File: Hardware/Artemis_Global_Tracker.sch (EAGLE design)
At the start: 137 parts, among them J1 IRIDIUM_9603N, J2 USB-C, J6 U.FL, J7 ANTENNA-GROUNDEDEDGE_SMA, Q1 DMG3414U-7, Q2 DMG3415U-7, Q3 DMG3415U-7, Q4 600mA/40V, U1 CH340E_MSOP10, U10 3.3V, U2 LTC3225EDDB#TRMPBF, U3 ADM4210-1, U4 UBLOX_ZOE_M8-0-10, U5 AS179-92LF, U6 MS8607-02BA01, U7 ARTEMIS_MODULESMD, U8 V_SUPERVISORBD48K24G-TL, U9 MCP73831, X1 32.768kHz, X2 32.768kHz

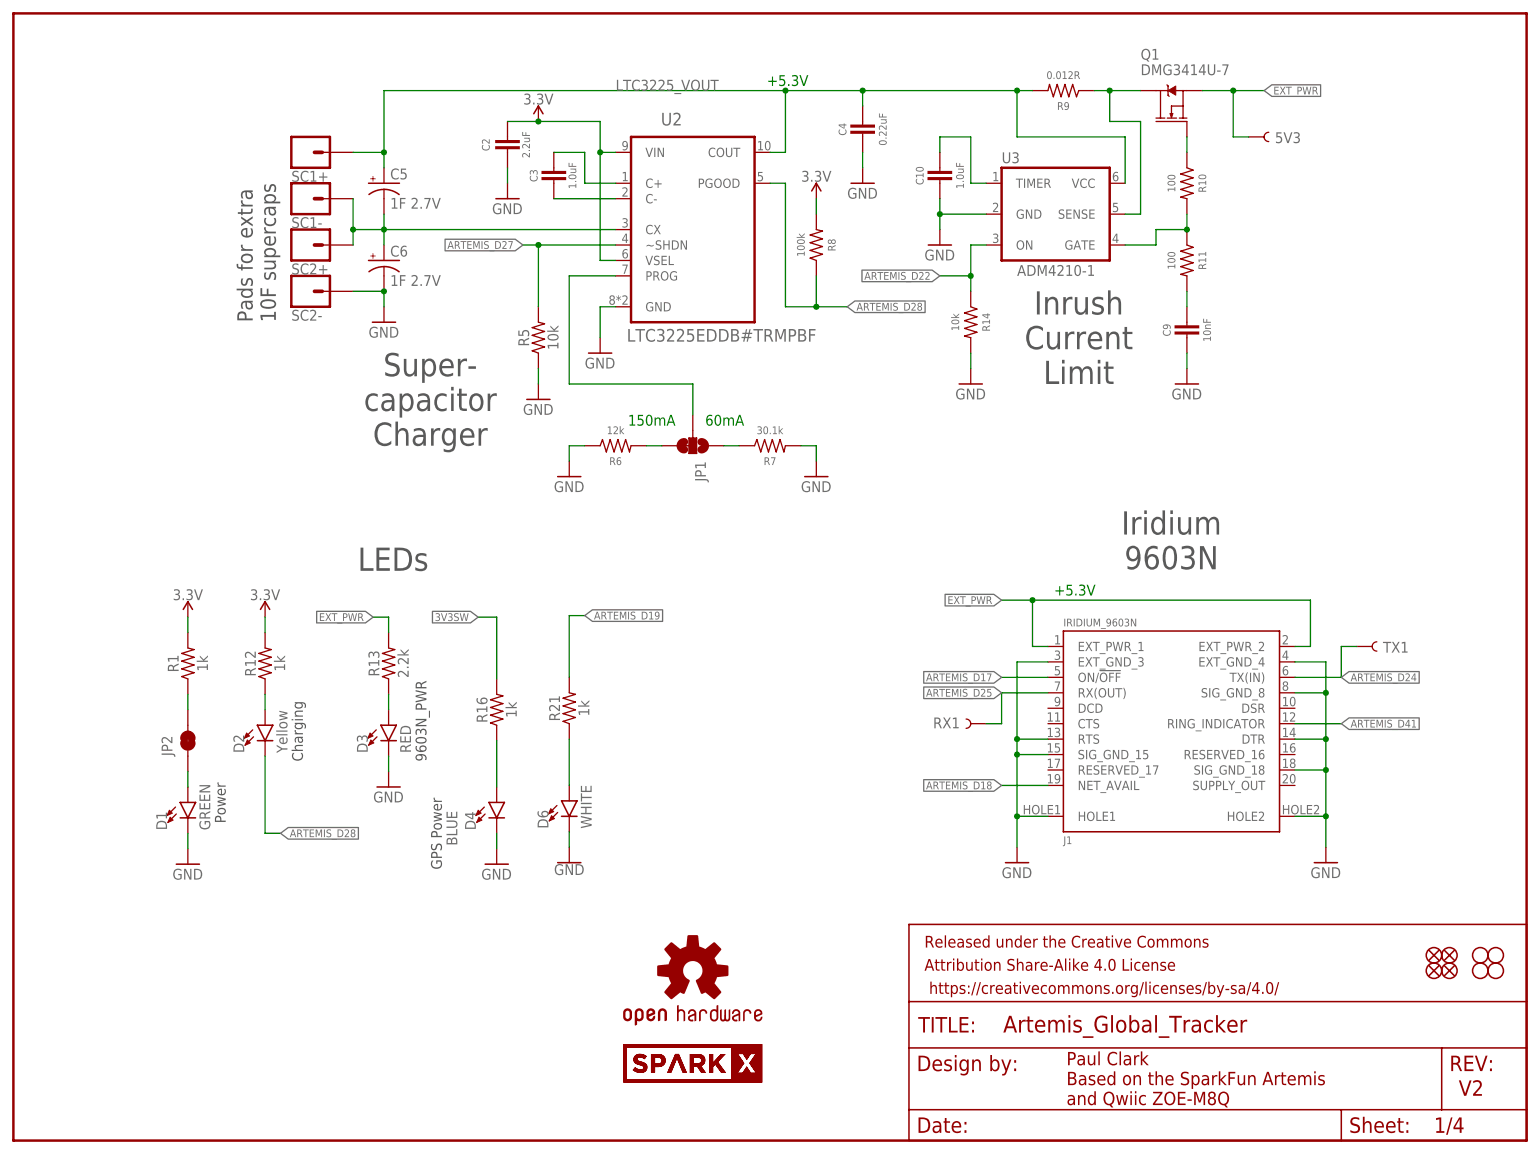
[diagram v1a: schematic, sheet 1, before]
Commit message: PROD_ID updates
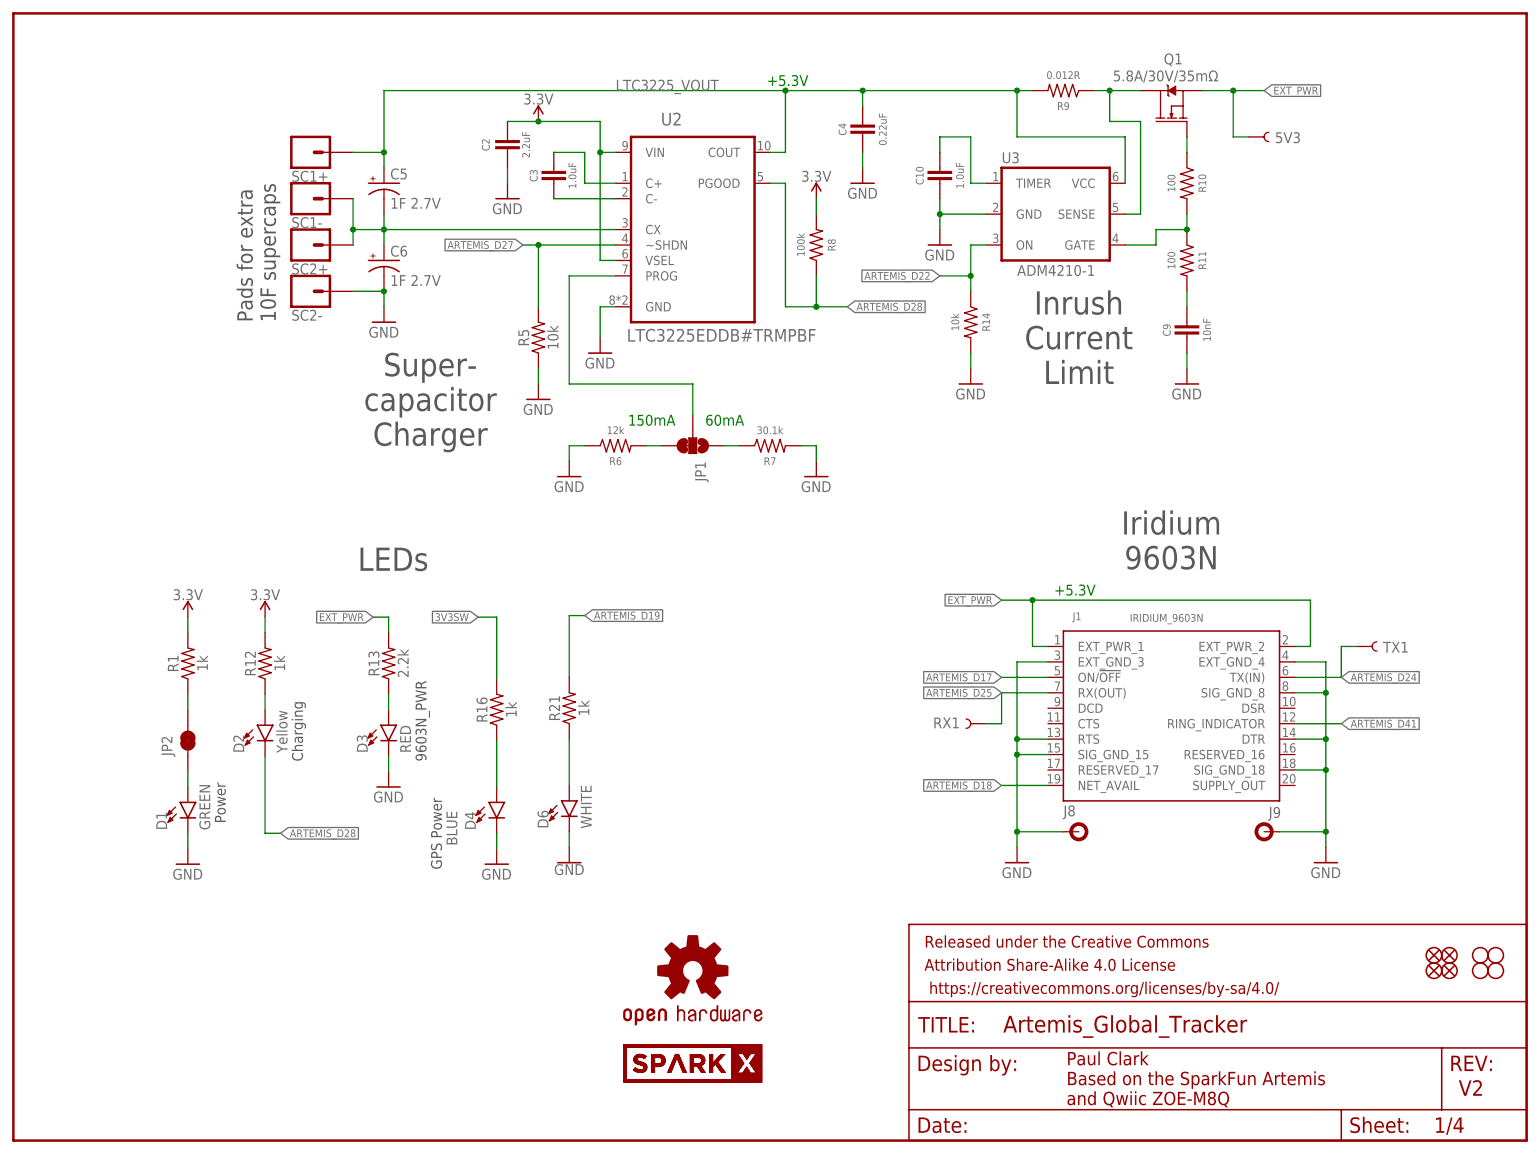
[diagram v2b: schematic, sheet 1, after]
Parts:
- added J8, J9: STANDOFFS_M2X0.4_STEEL_6MM, New_Parts:STANDOFFS_M2X0.4_STEEL_6MM
- C5, C6: device SparkFun-Capacitors:1F-2.7V(PTH)CPOL-RADIAL-1H-2.7V -> New_Parts:1F-2.7V(PTH)CPOL-RADIAL-1H-2.7V
- J2: device SparkFun-Connectors:USB_C2-LAYER -> SparkFun-Connectors:USB_C_2-LAYER
- Q1: value DMG3414U-7 -> 5.8A/30V/35mΩ; device New_Parts:DMG3414U-7 -> SparkFun-DiscreteSemi:MOSFET-NCH-AO3404A
- Q2, Q3: value DMG3415U-7 -> 20V/4.2A/52mΩ/1.4W; device New_Parts:DMG3415U -> SparkFun-DiscreteSemi:MOSFET_PCH-DMG2305UX-7
- U4: value UBLOX_ZOE_M8-0-10 -> U-BLOX_ZOE_M8Q-0-10; device SparkFun-GPS:UBLOX_ZOE_M8-0-10 -> SparkFun-GPS:U-BLOX_ZOE_M8Q-0-10
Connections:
- net GND: now also J8.1, J9.1; no longer J1.HOLE1, J1.HOLE2
